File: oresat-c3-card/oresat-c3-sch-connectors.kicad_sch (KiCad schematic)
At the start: 29 parts, among them J1 TFM-120-01-L-D-RA, J2 2-1734592-0, J3 733000020, J4 733000020

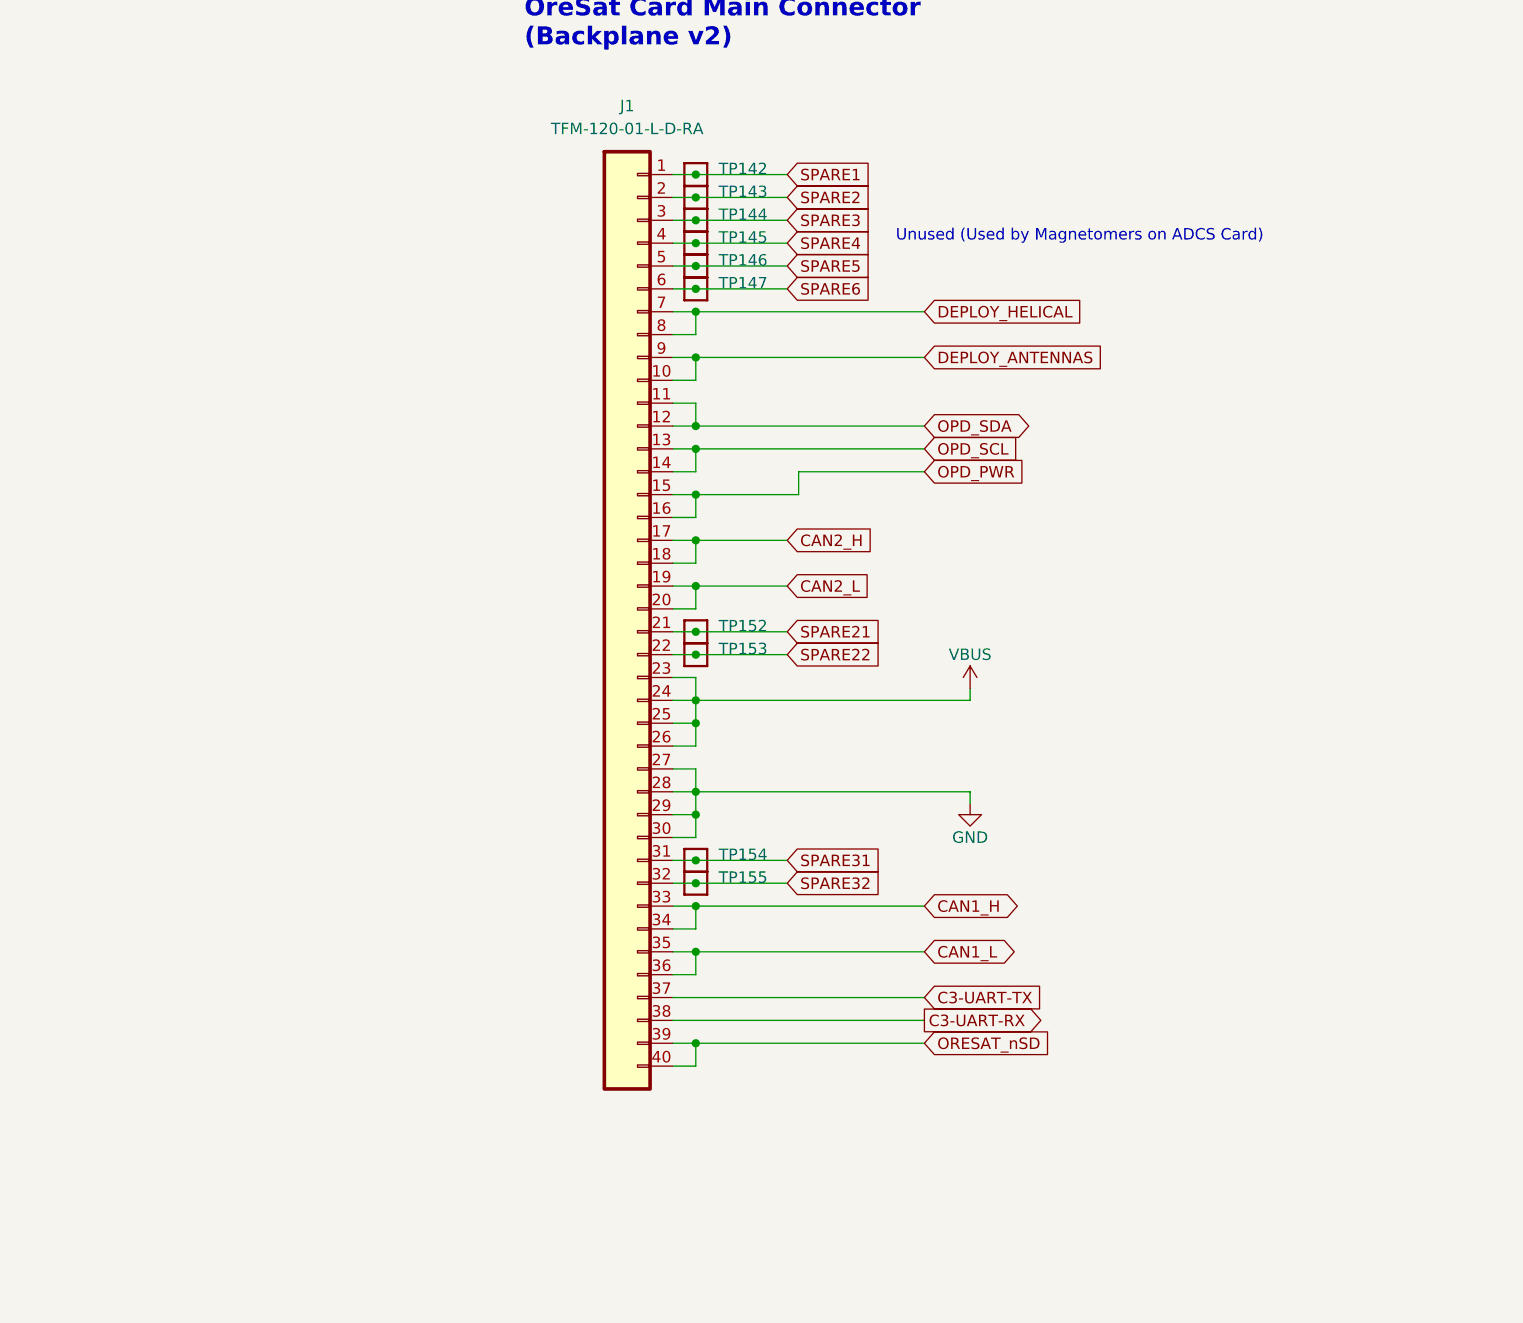
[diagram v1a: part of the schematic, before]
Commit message: schematic changes following design review
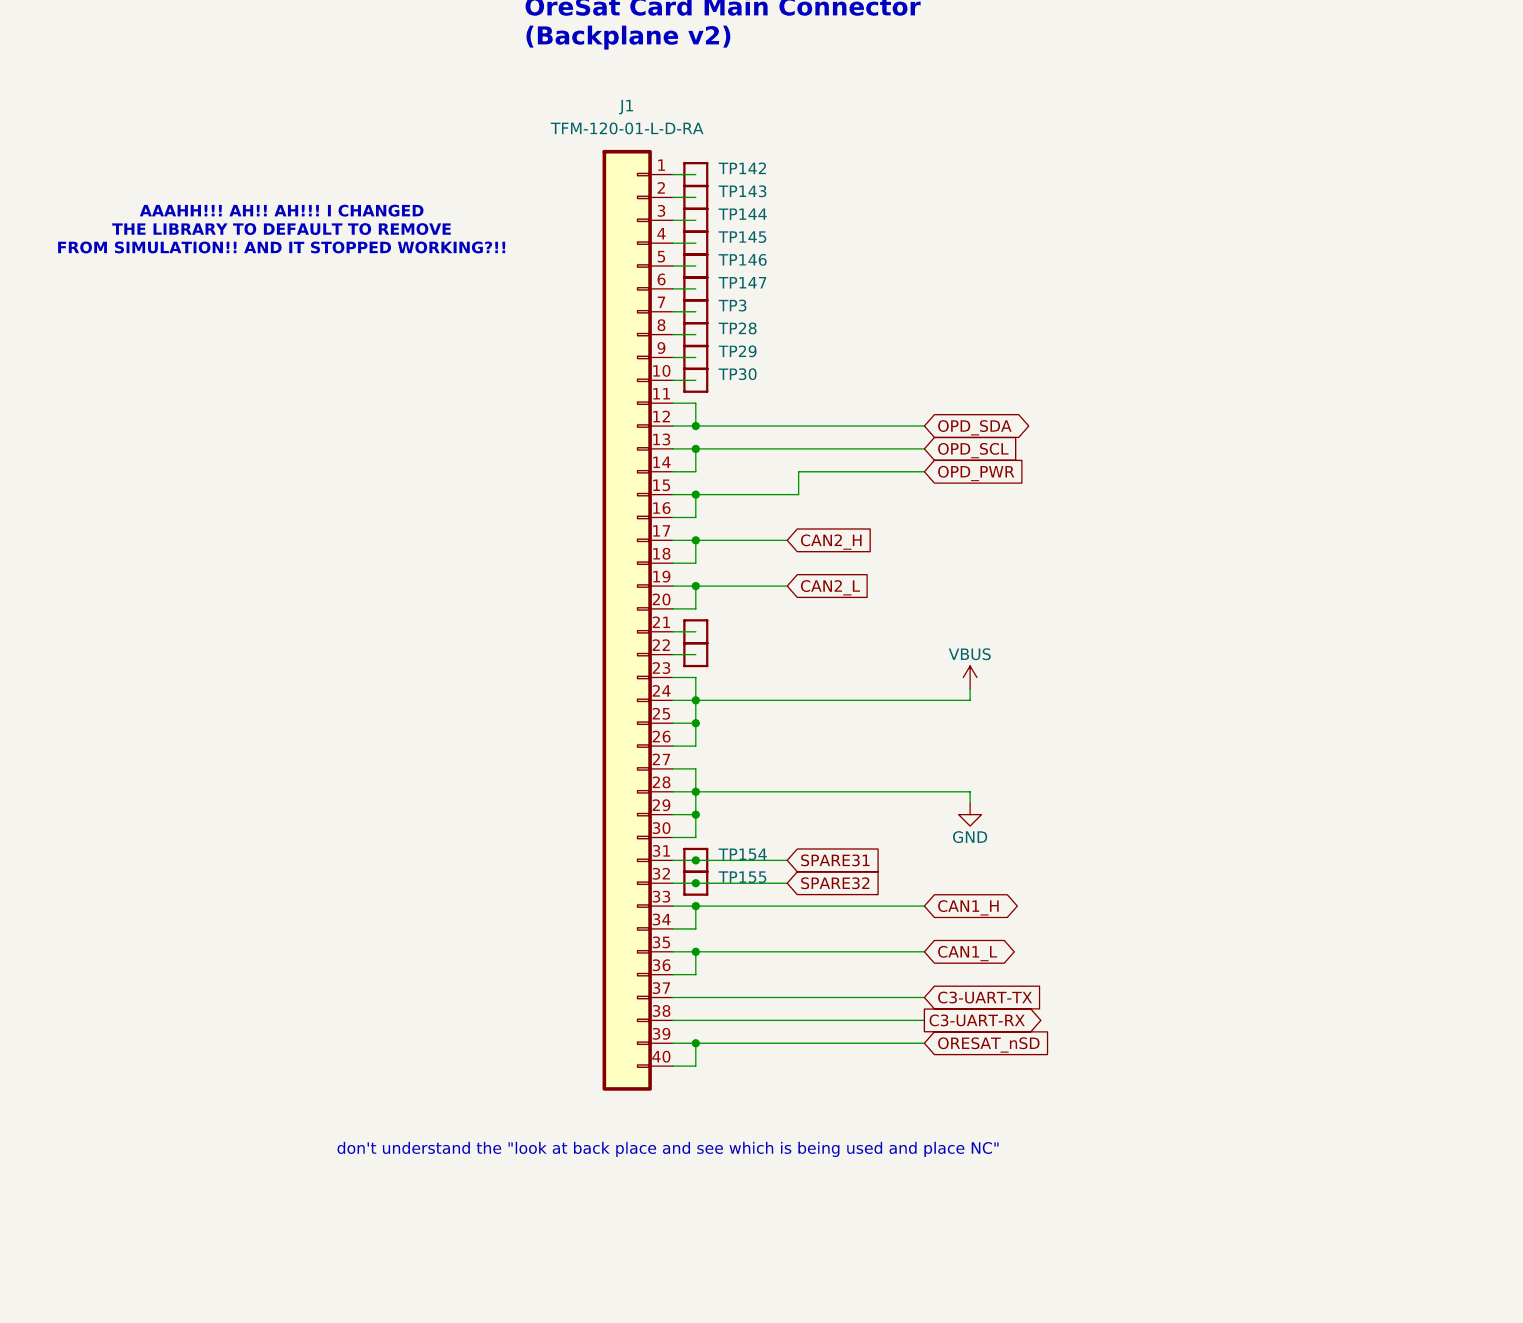
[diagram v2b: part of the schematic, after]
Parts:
- added TP28, TP29, TP3, TP30: Test-Point, oresat-misc:TestPoint_Pad_D1.0mm, symbol oresat-misc:Test-Point-1mm-round
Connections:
- net DEPLOY_ANTENNAS: no longer names the net of J1.9
- net DEPLOY_ANTENNAS: now also TP29.1; no longer J1.10
- net DEPLOY_HELICAL: no longer names the net of J1.7
- net DEPLOY_HELICAL: now also TP3.1; no longer J1.8
- net SPARE1: no longer names the net of J1.1, TP142.1
- net SPARE2: no longer names the net of J1.2, TP143.1
- net SPARE21: no longer names the net of J1.21, TP152.1
- net SPARE22: no longer names the net of J1.22, TP153.1
- net SPARE3: no longer names the net of J1.3, TP144.1
- net SPARE4: no longer names the net of J1.4, TP145.1
- net SPARE5: no longer names the net of J1.5, TP146.1
- net SPARE6: no longer names the net of J1.6, TP147.1
- new net: J1.10, TP30.1
- new net: J1.8, TP28.1
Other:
- note added: "AAAHH!!! AH!! AH!!! I CHANGED THE LIBRARY TO DEFAULT TO REMOVE FROM SIMULATION!! AND IT STOPPED WORKING?!!"
- note added: "don't understand the "look at back place and see which is being used and place NC""
- note removed: "Unused (Used by Magnetomers on ADCS Card)"

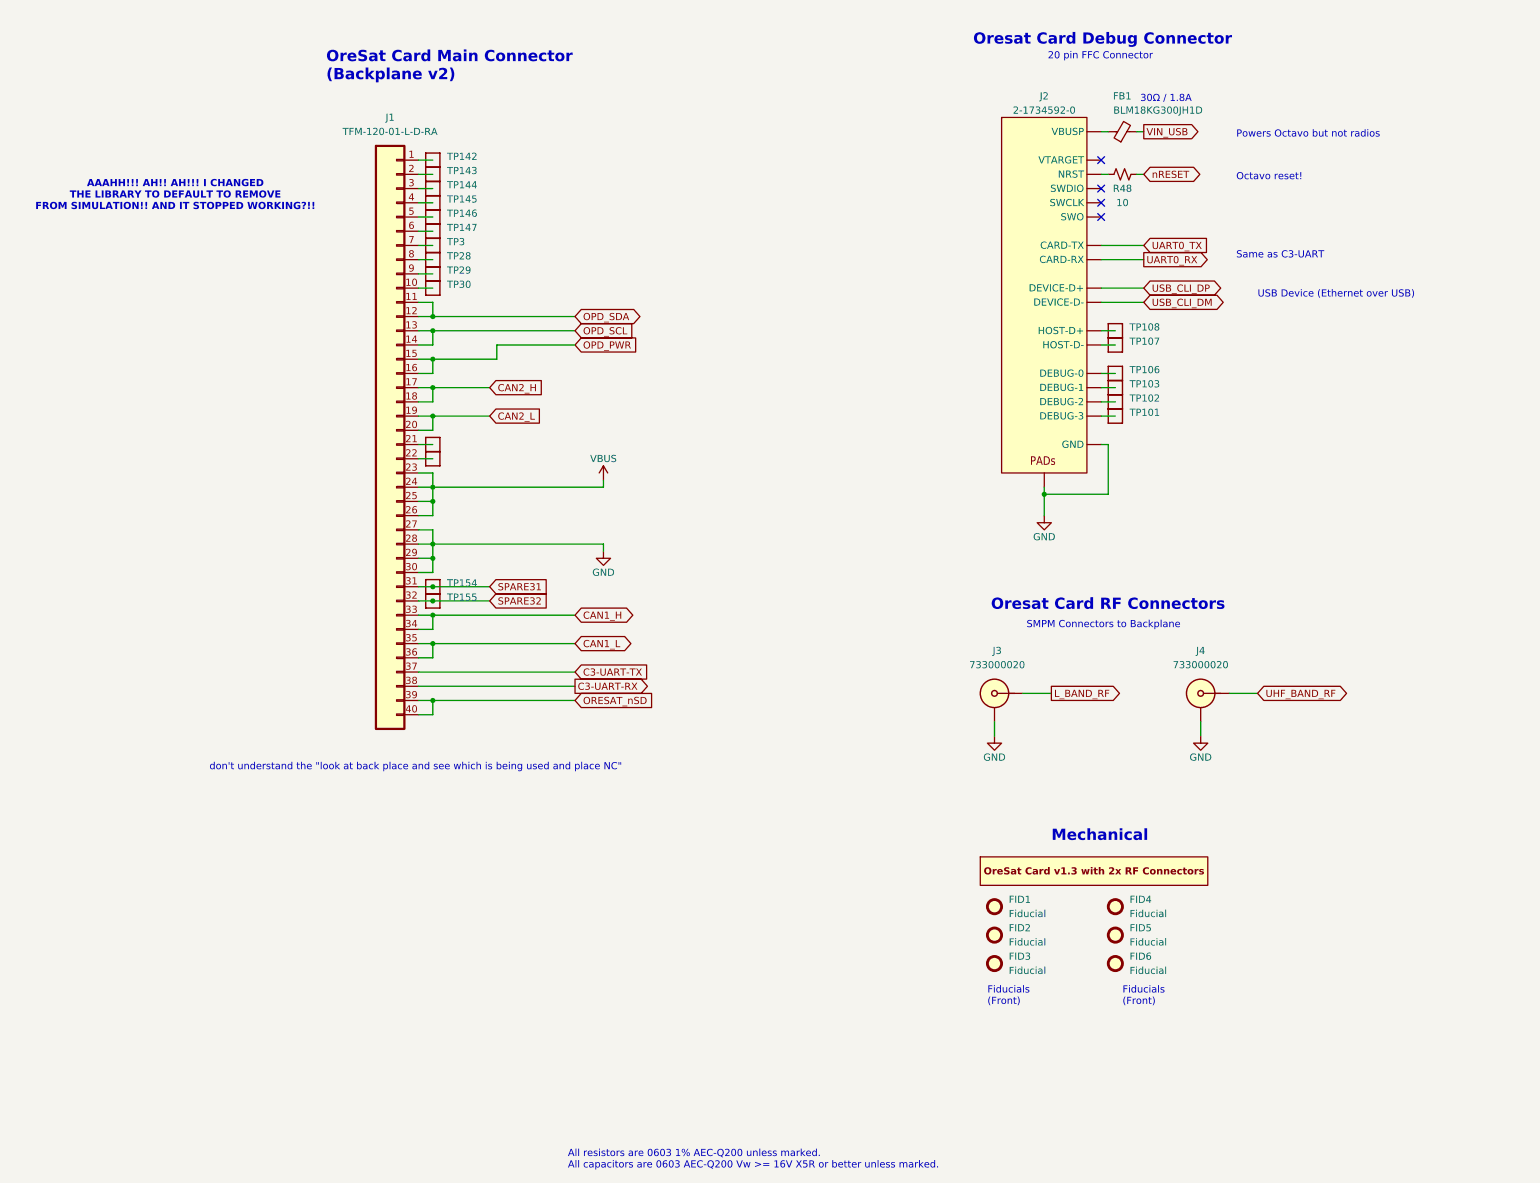
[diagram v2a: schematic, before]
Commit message: Additional C3 design review changes and routing progress
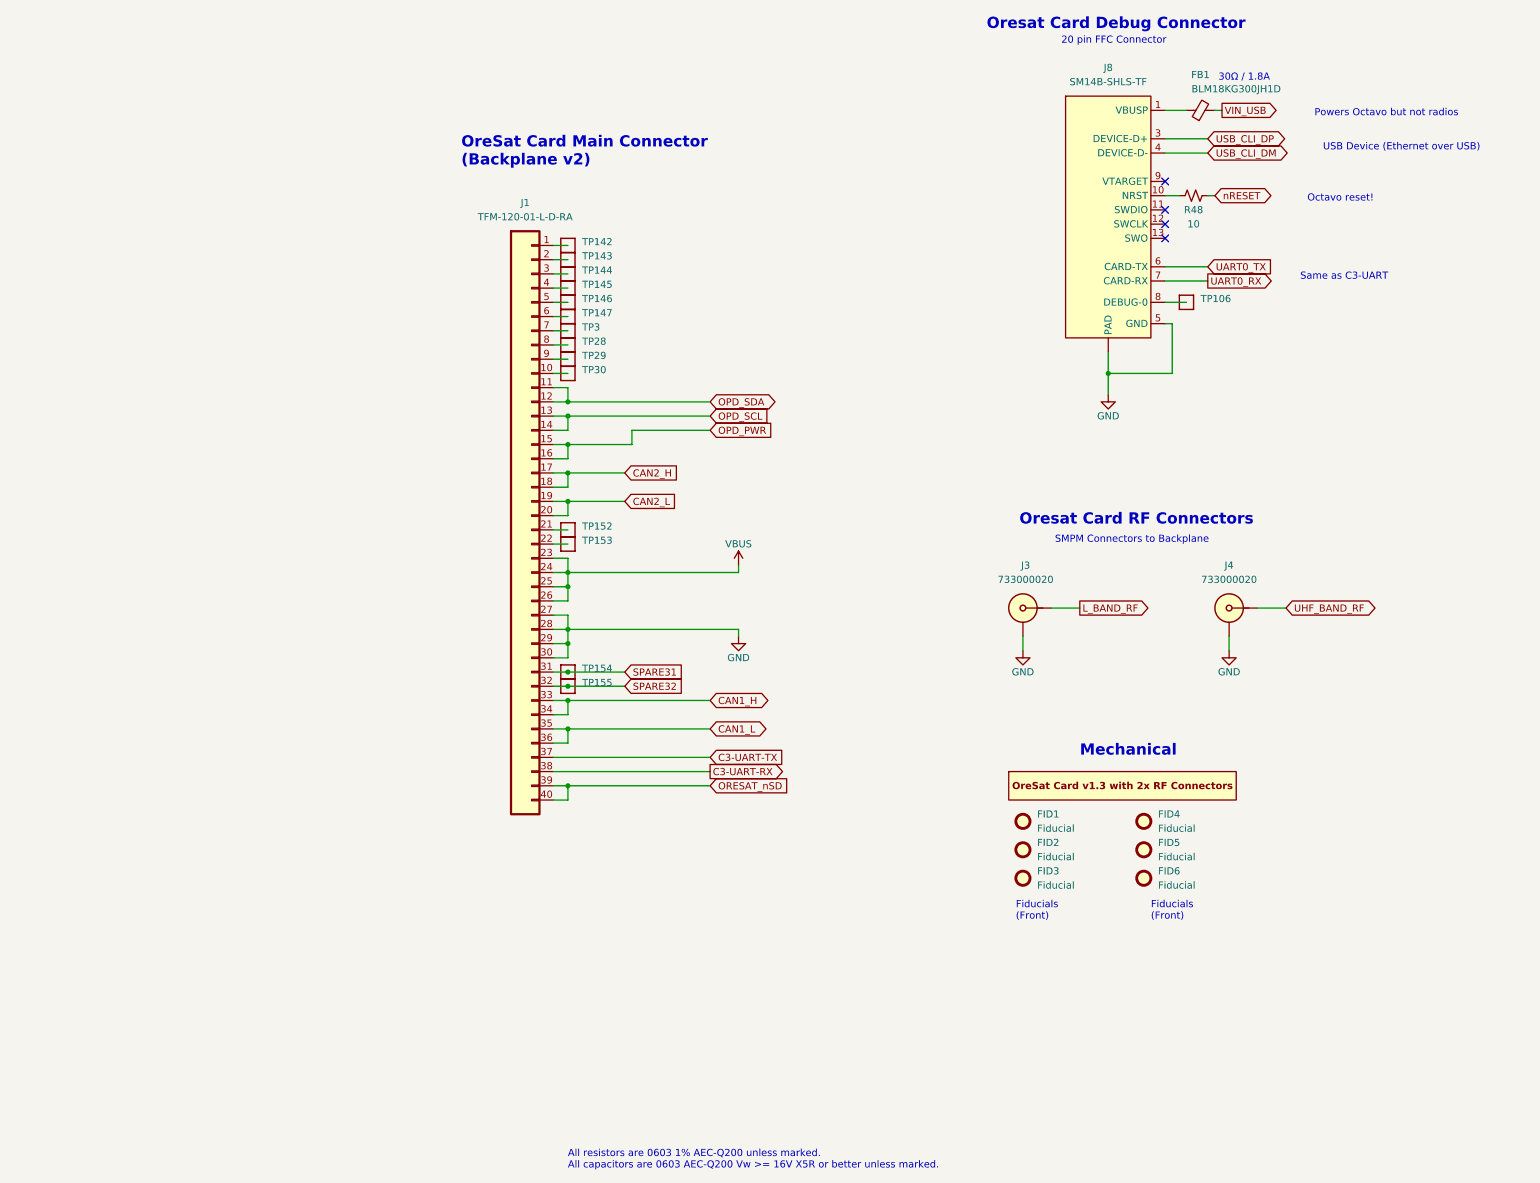
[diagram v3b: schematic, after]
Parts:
- removed J2: 2-1734592-0, oresat-connectors:J-TE-2-1734592-0, symbol oresat-connectors:J-TE-2-1734592-0
- removed TP101, TP102, TP103, TP107, TP108: Test-Point, oresat-misc:TestPoint_Pad_D1.0mm, symbol oresat-misc:Test-Point-1mm-round
- added J8: SM14B-SHLS-TF, oresat-connectors:J-JST-SM14BSHLSTF, symbol oresat-connectors:ORESAT-DEBUG-CONNECTOR-3
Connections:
- net GND: now also J8.14 (GND), J8.15 (PAD), J8.16 (PAD), J8.5 (GND)
- net UART0_RX: now also J8.7 (CARD-RX)
- net UART0_TX: now also J8.6 (CARD-TX)
- net USB_CLI_DM: now also J8.4 (DEVICE-D-)
- net USB_CLI_DP: now also J8.3 (DEVICE-D+)
- net at FB1.1: now also J8.1 (VBUSP), J8.2 (VBUSP)
- net at R48.1: now also J8.10 (NRST)
- net at TP106.1: now also J8.8 (DEBUG-0)
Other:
- note removed: "AAAHH!!! AH!! AH!!! I CHANGED THE LIBRARY TO DEFAULT TO REMOVE FROM SIMULATION!! AND IT STOPPED WORKING?!!"
- note removed: "don't understand the "look at back place and see which is being used and place NC""
- moved on the sheet: FB1, FID1, FID2, FID3, FID4, FID5, FID6, J1, J3, J4, R48, TP106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

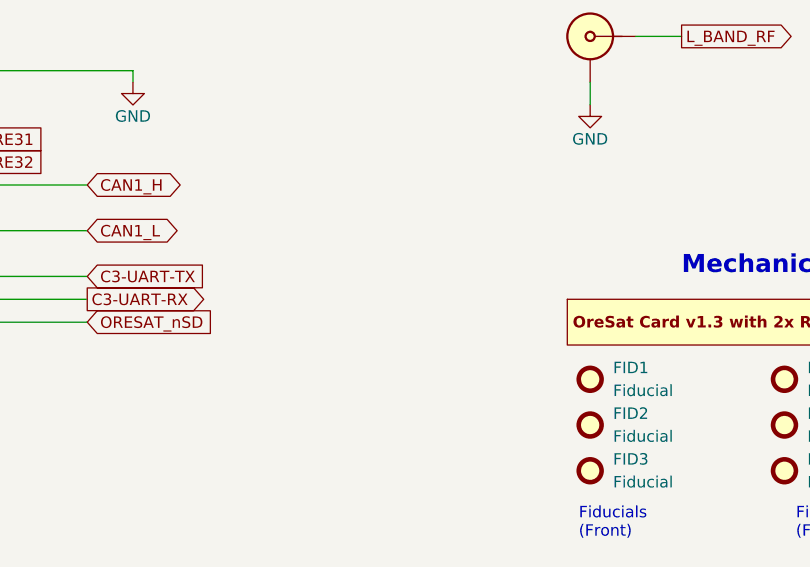
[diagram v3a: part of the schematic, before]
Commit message: completed rough rounting on left side and l band rf side
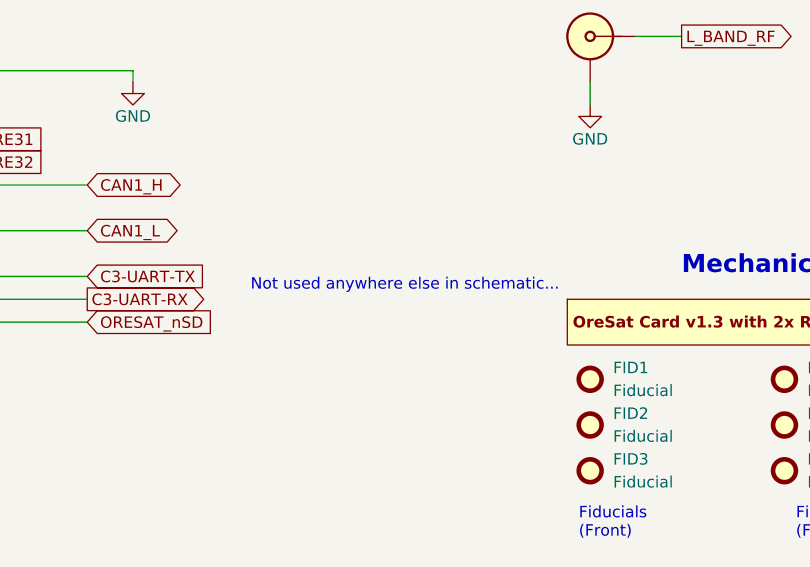
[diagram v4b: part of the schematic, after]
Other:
- note added: "Not used anywhere else in schematic..."
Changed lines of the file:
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@@
+		)
+	)
+	(text "Not used anywhere else in schematic..."
+		(exclude_from_sim no)
+		(at 176.276 188.976 0)
+		(effects
+			(font
+				(size 1.27 1.27)
+			)
 		)
 	)
